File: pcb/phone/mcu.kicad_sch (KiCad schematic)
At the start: 22 parts, among them U1 STM32H743ZIT6, Y1 ECS-80-12-33Q-GN-TR

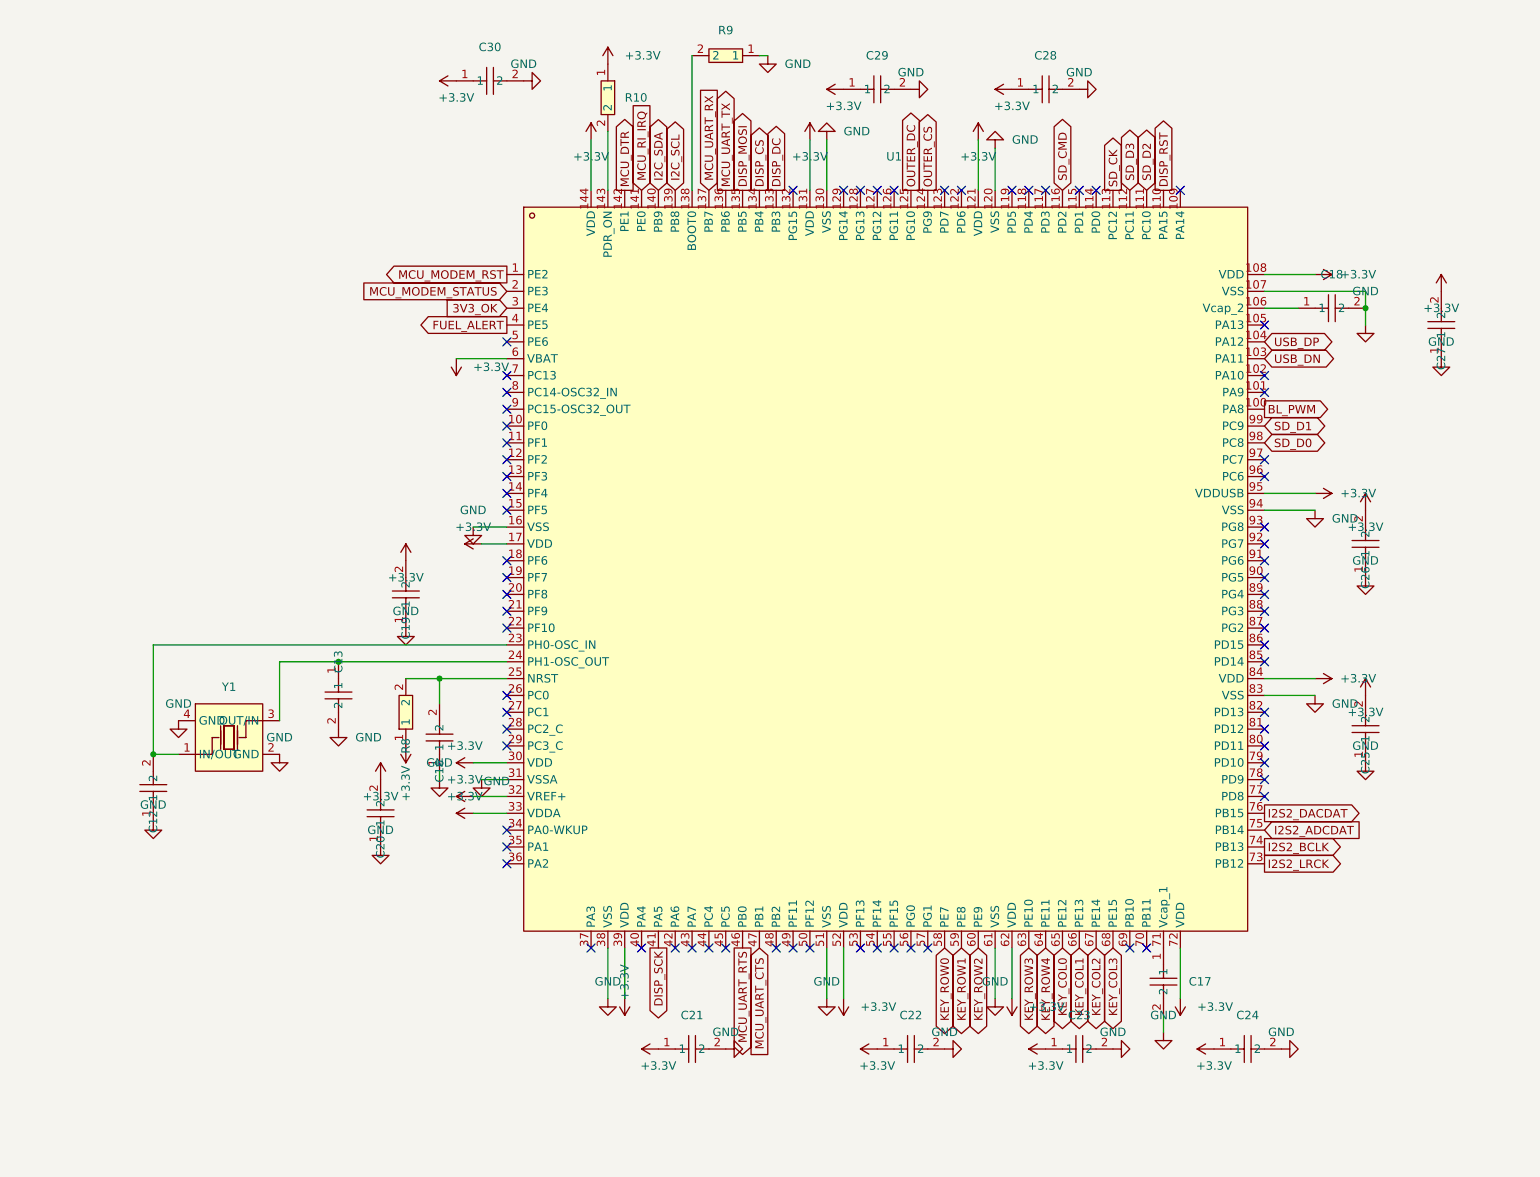
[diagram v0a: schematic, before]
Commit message: Add deferred components: VBUS divider, MCU_MODEM_PWR_EN pull-down, SWD header, NET_STATUS LED
MCU sheet:
- R11 (10k): MCU_MODEM_PWR_EN pull-down to GND
- R12 (100k) + R13 (47k): VBUS_SENSE voltage divider from VBUS to GND
- J3 (Conn_01x04): SWD programming header (SWCLK, SWDIO, +3.3V, GND)
- Removed 4 no_connect markers (MCU_MODEM_PWR_EN, VBUS_SENSE, SWCLK, SWDIO)

Modem sheet:
- R12 (1k) + LED1 (LTST-C191TBKT): NET_STATUS indicator LED
- Removed 1 no_connect marker (NET_STATUS)

ERC: 0 errors, 4 warnings (all lib_symbol_mismatch — 3 pre-existing + 1 new for J3)

Generated with [Devin](https://devin.ai)

Co-Authored-By: Devin <158243242+devin-ai-integration[bot]@users.noreply.github.com>
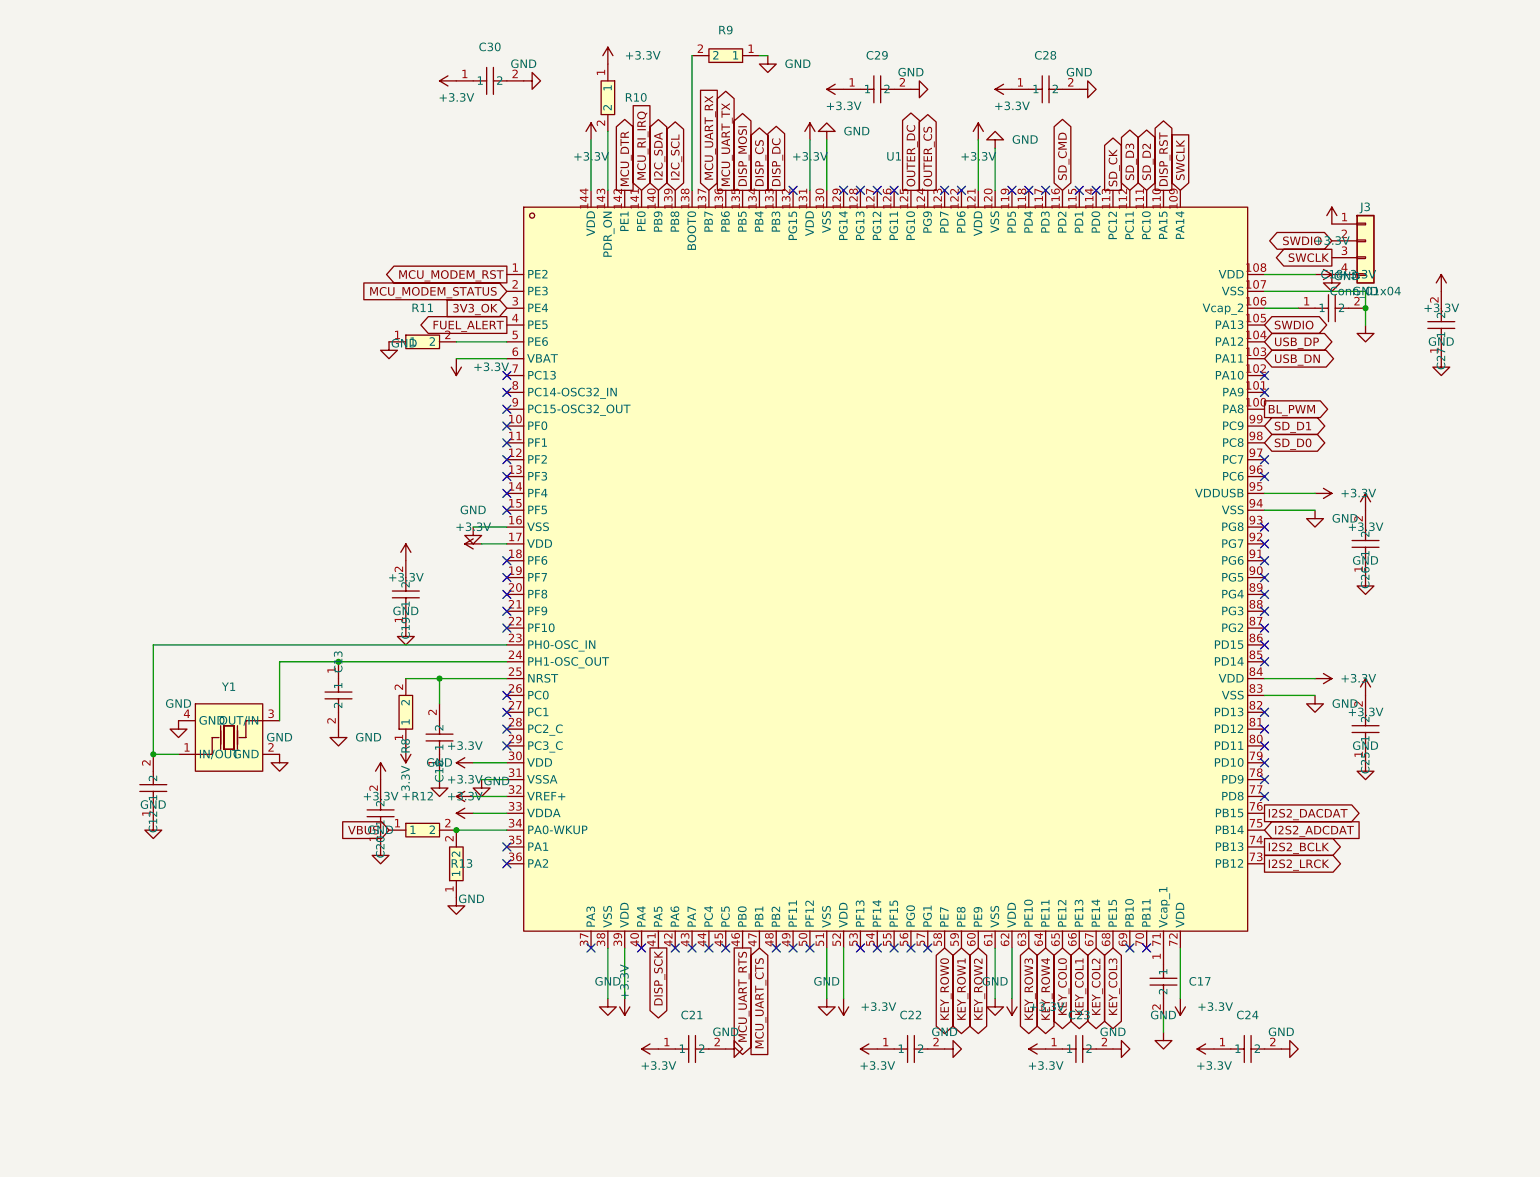
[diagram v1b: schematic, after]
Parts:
- added J3: Conn_01x04, symbol Connector_Generic:Conn_01x04
- added R11: 10k, easyeda2kicad:R0603, symbol passives:RC0603JR-0710KL
- added R12: 100k, easyeda2kicad:R0603, symbol passives:RC0603JR-0710KL
- added R13: 47k, easyeda2kicad:R0603, symbol passives:RC0603JR-0710KL
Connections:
- net +3.3V: now also J3.1 (Pin_1)
- net GND: now also J3.4 (Pin_4), R11.1, R13.1
- net SWDIO: now reaches U1.105 (PA13)
- net SWDIO: now also J3.2 (Pin_2)
- net SWCLK: now reaches U1.109 (PA14)
- net SWCLK: now also J3.3 (Pin_3)
- net at U1.34 (PA0-WKUP): now also R12.2, R13.2
- net at U1.5 (PE6): now also R11.2
- new net VBUS: R12.1
- no-connect marks 71 -> 67

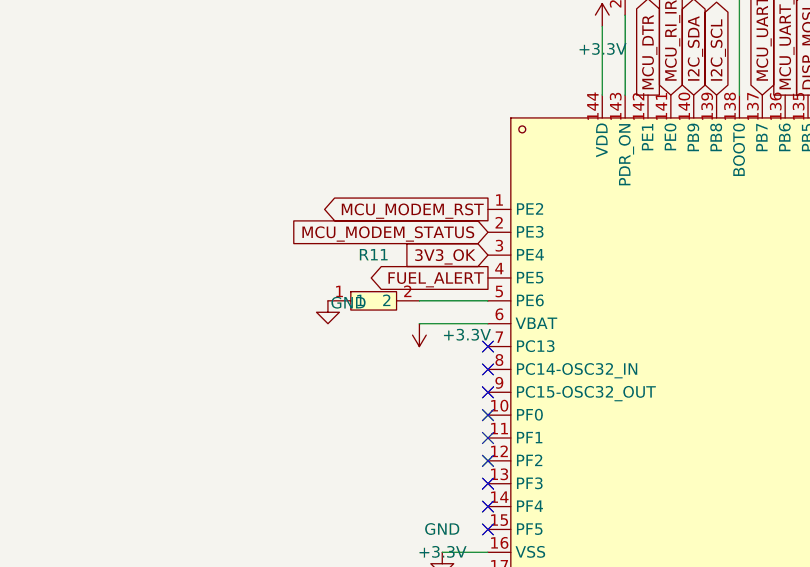
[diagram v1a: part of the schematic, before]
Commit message: Add power slide switch, modem bulk caps, reverse load switch decision
- SW1 (ALPS SSSS811101) added to power sheet: controls TPS63021 EN pin
  (ON: +BATT->R1->SW1->EN, OFF: EN->SW1->GND). Allows charging while off.
- C40 (470uF tantalum) + C41/C42 (10uF ceramic) added to modem sheet
  near MPCIe VCC pins for 2A+ LTE burst handling.
- Reversed load switch decision: SIM7600 sleep mode + PWRKEY make it
  redundant. Removed R11 (MCU_MODEM_PWR_EN pull-down), added no_connect
  on PE6.
- Registered temp_switch/temp_470uf/temp_10uf libraries in sym-lib-table
  and fp-lib-table (resolves 3 library-link ERC warnings).
- Final ERC: 0 errors, 6 warnings (all lib_symbol_mismatch, harmless).
- Updated docs: project-log, task-tracker, bom.

Generated with [Devin](https://devin.ai)

Co-Authored-By: Devin <158243242+devin-ai-integration[bot]@users.noreply.github.com>
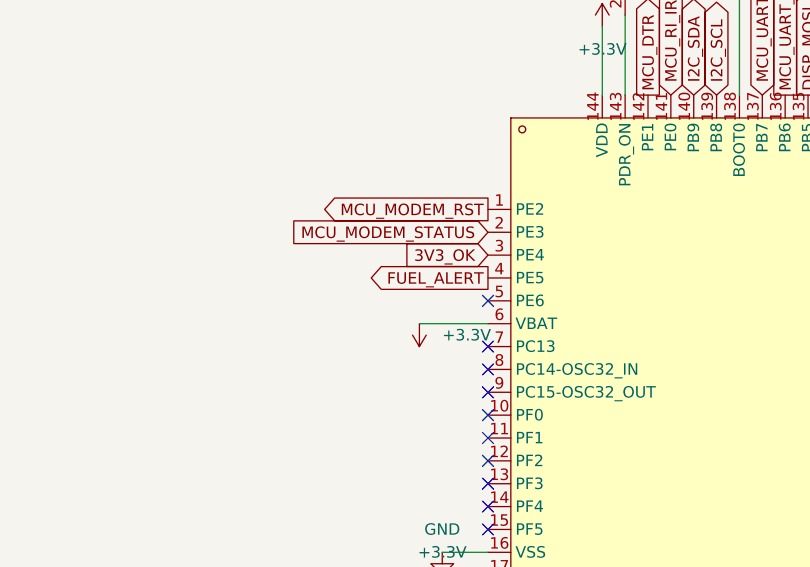
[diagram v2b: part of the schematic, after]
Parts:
- removed R11: 10k, easyeda2kicad:R0603, symbol passives:RC0603JR-0710KL
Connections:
- no-connect marks 67 -> 68
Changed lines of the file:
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@@
 	)
 	(no_connect
+		(at 172.72 101.6)
+	)
+	(no_connect
 		(at 172.72 106.68)
 	)
@@
 		)
 	)
-	(wire
-		(pts
-			(xy 165.1 101.6) (xy 172.72 101.6)
-		)
-		(stroke
-			(width 0)
-			(type default)
-		)
-	)
 	(global_label "I2S2_BCLK"
 		(shape output)
@@
 	(symbol
 		(lib_id "passives:RC0603JR-0710KL")
-		(at 160.02 101.6 0)
-		(unit 1)
-		(body_style 1)
-		(exclude_from_sim no)
-		(in_bom yes)
-		(on_board yes)
-		(in_pos_files yes)
-		(dnp no)
-		(fields_autoplaced yes)
-		(property "Reference" "R11"
-			(at 160.02 96.52 0)
-			(show_name no)
-			(do_not_autoplace no)
-			(effects
-				(font
-					(size 1.27 1.27)
-				)
-			)
-		)
-		(property "Value" "10k"
-			(at 160.02 106.68 0)
-			(hide yes)
-			(show_name no)
-			(do_not_autoplace no)
-			(effects
-				(font
-					(size 1.27 1.27)
-				)
-			)
-		)
-		(property "Footprint" "easyeda2kicad:R0603"
-			(at 160.02 101.6 0)
-			(hide yes)
-			(show_name no)
-			(do_not_autoplace no)
-			(effects
-				(font
-					(size 1.27 1.27)
-				)
-			)
-		)
-		(property "Datasheet" ""
-			(at 160.02 101.6 0)
-			(hide yes)
-			(show_name no)
-			(do_not_autoplace no)
-			(effects
-				(font
-					(size 1.27 1.27)
-				)
-			)
-		)
-		(property "Description" ""
-			(at 160.02 101.6 0)
-			(hide yes)
-			(show_name no)
-			(do_not_autoplace no)
-			(effects
-				(font
-					(size 1.27 1.27)
-				)
-			)
-		)
-		(pin "2"
-		)
-		(pin "1"
-		)
-		(instances
-			(project "phone"
-				(path "/451c3b43-1616-42cb-bf96-d436f4db82c2/d692f43a-094c-48db-863f-ce7b80cfd81e"
-					(reference "R11")
-					(unit 1)
-				)
-			)
-		)
-	)
-	(symbol
-		(lib_id "passives:RC0603JR-0710KL")
 		(at 160.02 175.26 0)
 		(unit 1)
@@
 					(unit 1)
 				)
-			)
-		)
-	)
-	(symbol
-		(lib_id "power:GND")
-		(at 154.94 101.6 0)
-		(unit 1)
-		(body_style 1)
-		(exclude_from_sim no)
-		(in_bom yes)
-		(on_board yes)
-		(in_pos_files yes)
-		(dnp no)
-		(fields_autoplaced yes)
-		(property "Reference" "#PWR83"
-			(at 156.21 99.05999999999999 0)
-			(hide yes)
-			(show_name no)
-			(do_not_autoplace no)
-			(effects
-				(font
-					(size 1.27 1.27)
-				)
-			)
-		)
-		(property "Value" "GND"
-			(at 157.226 101.854 0)
-			(show_name no)
-			(do_not_autoplace no)
-			(effects
-				(font
-					(size 1.27 1.27)
-				)
-			)
-		)
-		(property "Footprint" ""
-			(at 154.94 101.6 0)
-			(hide yes)
-			(show_name no)
-			(do_not_autoplace no)
-			(effects
-				(font
-					(size 1.27 1.27)
-				)
-			)
-		)
-		(property "Datasheet" ""
-			(at 154.94 101.6 0)
-			(hide yes)
-			(show_name no)
-			(do_not_autoplace no)
-			(effects
-				(font
-					(size 1.27 1.27)
-				)
-			)
-		)
-		(property "Description" "Power symbol creates a global label with name \"GND\" , ground"
-			(at 154.94 101.6 0)
-			(hide yes)
-			(show_name no)
-			(do_not_autoplace no)
-			(effects
-				(font
-					(size 1.27 1.27)
-				)
-			)
-		)
-		(pin "1"
-		)
-		(instances
-			(project "phone"
-				(path "/451c3b43-1616-42cb-bf96-d436f4db82c2/d692f43a-094c-48db-863f-ce7b80cfd81e"
-					(reference "#PWR83")
-					(unit 1)
-				)
